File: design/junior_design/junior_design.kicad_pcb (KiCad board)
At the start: 2 copper layers, 28 parts, among them J1 MPLAB SNAP, J2 Screw_Terminal_01x04, J3 Conn_01x05, J4 Conn_01x03, J5 USB_C_Receptacle_USB2.0_16P, U2 INA128, U3 TLV76133DCY, U4 MCP6022

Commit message: Started PCB layout
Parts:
- added H1: MountingHole, MountingHole:MountingHole_2.7mm, F.Cu at (76.2, 76.2)
- added H2: MountingHole, MountingHole:MountingHole_2.7mm, F.Cu at (196.8, 76.2)
- added H3: MountingHole, MountingHole:MountingHole_2.7mm, F.Cu at (76.2, 158.8)
- added H4: MountingHole, MountingHole:MountingHole_2.7mm, F.Cu at (196.8, 158.8)
- added U100: PIC24FJ64GA002-I_SP, Package_DIP:DIP-28_W7.62mm, F.Cu at (131.4, 133.3)
- moved R190 78.9 mm to (75.7, 122.4)
- moved U190 75.2 mm to (88.9, 116.2)
- moved J100 74.1 mm to (197.6, 106.1)
- moved R191 73.1 mm to (79.4, 112.4), turned to 90 degrees
- moved U110 71.3 mm to (158.1, 144.8), turned to 180 degrees
- moved U130 68.3 mm to (131.4, 139.7)
- moved J111 64.8 mm to (168.3, 150.5), turned to 90 degrees
- moved RV131 63.8 mm to (127.0, 147.8), turned to -90 degrees
- moved C190 62.3 mm to (83.2, 116.2), turned to 90 degrees
- moved J121 56.9 mm to (169.5, 132.1), turned to 180 degrees
- moved J190 55.6 mm to (77.4, 113.1), turned to -90 degrees
- moved C191 55.5 mm to (90.8, 120.7), turned to 180 degrees
- moved C111 52.6 mm to (173.4, 148.6), turned to -90 degrees
- moved RV130 51.7 mm to (144.3, 150.4), turned to -90 degrees
- moved R133 51.2 mm to (127.5, 140.2)
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- renumbered C1 to C100, C2 to C101, C3 to C102, C7 to C110, C6 to C111, C9 to C121, C8 to C130, C4 to C190, C5 to C191, J1 to J100, J2 to J111, J3 to J120, J4 to J121, J5 to J190, R7 to R100, R6 to R101, R1 to R110, R2 to R130, R4 to R131, R3 to R132, R5 to R133, R8 to R190, R9 to R191, RV2 to RV130, RV1 to RV131, U2 to U110, U4 to U130, U3 to U190
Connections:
- J190 pad S1: unconnected-(J5-SHIELD-PadS1) -> GND
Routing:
- net GND: track 0.00 -> 22.1 mm, vias 0 -> 3
- net +5V: track 0.00 -> 14.9 mm
- net Net-(U100-AN1/VREF-/CN3/RA1): track 0.00 -> 12.5 mm
- net /LDCELL+: track 0.00 -> 10.4 mm
- net /LDCELL-: track 0.00 -> 10.4 mm
- net Net-(U100-AN0/VREF+/CN2/RA0): track 0.00 -> 9.94 mm
- net +3.3V: track 0.00 -> 8.37 mm
- net Net-(U100-AN5/C1IN+/RP3/SCL2/CN7/RB3): track 0.00 -> 7.93 mm
- net Net-(J190-CC2): track 0.00 -> 5.96 mm
- net Net-(J190-CC1): track 0.00 -> 4.09 mm, vias 0 -> 1
- net Net-(R110-Pad2): track 0.00 -> 3.96 mm
- net Net-(R110-Pad1): track 0.00 -> 3.94 mm
- added copper zone on F.Cu, net +3.3V
- added copper zone on F.Cu, net +5V
- added copper zone on B.Cu, net GND
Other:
- board outline added: 130.8 x 92.7 mm

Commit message: Finish routing PCB
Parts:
- added G***: LOGO, LOGO, F.Cu at (120.7, 88.3)
- added G***: LOGO, LOGO, B.Cu at (136.5, 116.8)
- J111: footprint Connector_Phoenix_MC:PhoenixContact_MCV_1,5_4-G-3.81_1x04_P3.81mm_Vertical -> Connector_Phoenix_MC:PhoenixContact_MC_1,5_4-G-3.81_1x04_P3.81mm_Horizontal
- moved C111 18.5 mm to (156.2, 155.6), turned to 180 degrees
- moved J111 16.3 mm to (154.4, 159.0), turned to 0 degrees
- moved J121 14.8 mm to (159.4, 121.3), turned to 90 degrees
- moved J120 14.0 mm to (134.6, 114.3)
- moved C121 10.8 mm to (160.7, 118.7), turned to 180 degrees
- moved C100 1.27 mm to (151.8, 122.6)
- moved C101 1.27 mm to (131.4, 122.6)
- moved R133 0.76 mm to (128.3, 140.2)
- moved C130 0.51 mm to (142.2, 139.7)
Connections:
- C121 pad 1: +3.3V -> +5V
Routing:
- net +5V: track 14.9 -> 103.9 mm, vias 0 -> 2
- net /~{RST}: track 0.00 -> 83.6 mm
- net /PGD: track 0.00 -> 66.6 mm
- net /PGC: track 0.00 -> 63.8 mm
- net +3.3V: track 8.37 -> 61.1 mm
- net /SCL0: track 0.00 -> 20.0 mm
- net /SDA0: track 0.00 -> 19.7 mm
- net GND: track 22.1 -> 35.2 mm, vias 3 -> 32
- net /LDCELL+: track 10.4 -> 22.5 mm
- net /LDCELL-: track 10.4 -> 18.4 mm
- net /ADC-: track 0.00 -> 5.49 mm
- net /ADC+: track 0.00 -> 4.66 mm
- net /PWM0: track 0.00 -> 4.45 mm
- net Net-(U100-~{MCLR}): track 0.00 -> 2.90 mm
- net Net-(R132-Pad1): track 0.00 -> 2.75 mm
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- added copper zone on F.Cu, net GND
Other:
- board text added: "HINKLE INC"

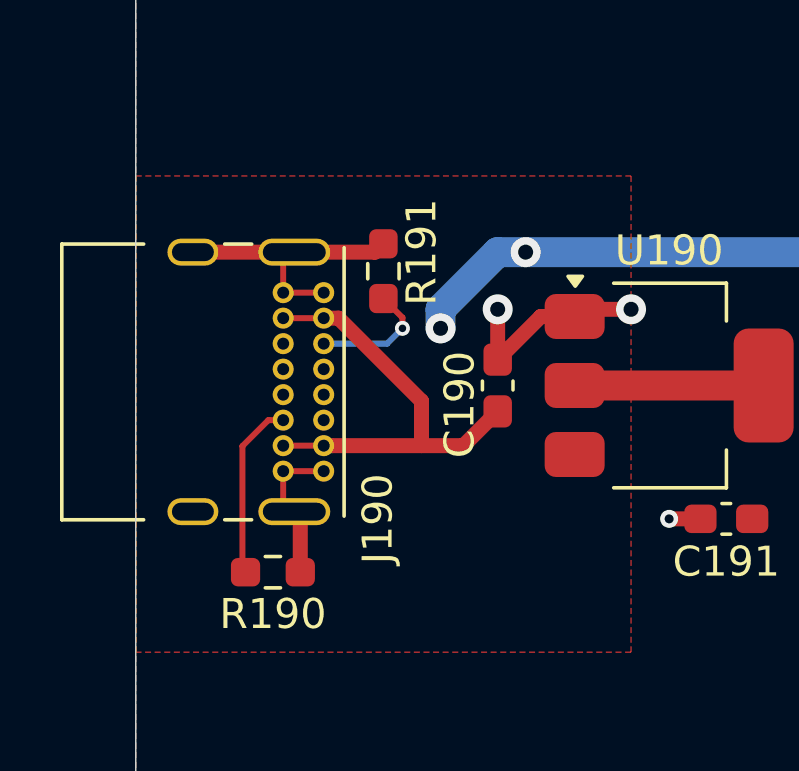
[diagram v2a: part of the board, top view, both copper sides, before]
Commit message: add ferrite beads to usb-c port
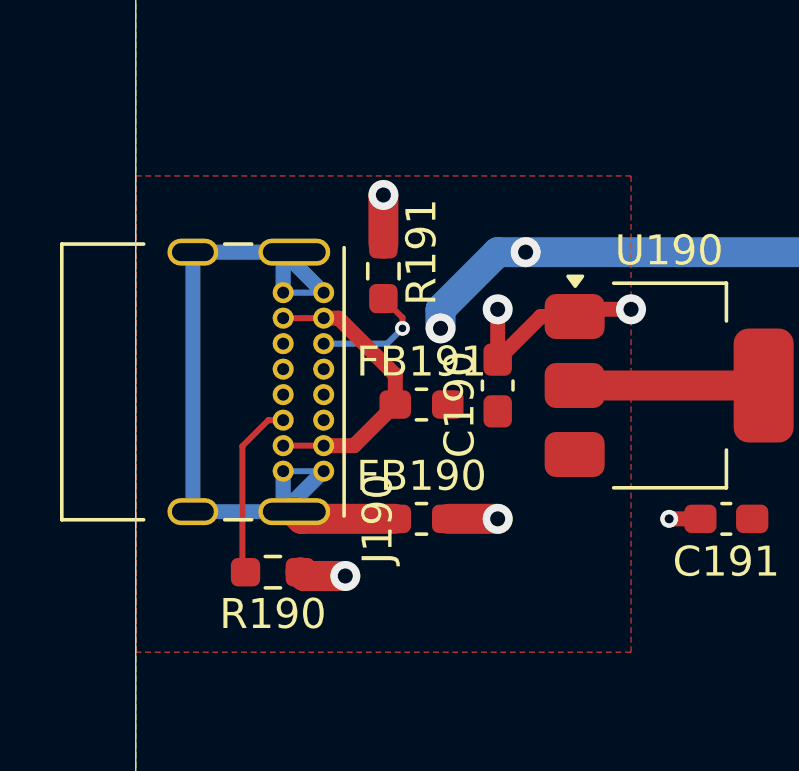
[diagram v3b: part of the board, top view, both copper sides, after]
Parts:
- added FB190: FerriteBead, Inductor_SMD:L_0603_1608Metric_Pad1.05x0.95mm_HandSolder, F.Cu at (80.6, 120.7)
- added FB191: FerriteBead, Inductor_SMD:L_0603_1608Metric_Pad1.05x0.95mm_HandSolder, F.Cu at (80.6, 116.8)
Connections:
- J190 pad A1: GND -> Net-(J190-SHIELD)
- J190 pad A12: GND -> Net-(J190-SHIELD)
- J190 pad A4: +5V -> Net-(FB191-Pad1)
- J190 pad A9: +5V -> Net-(FB191-Pad1)
- J190 pad B1: GND -> Net-(J190-SHIELD)
- J190 pad B12: GND -> Net-(J190-SHIELD)
- J190 pad B4: +5V -> Net-(FB191-Pad1)
- J190 pad B9: +5V -> Net-(FB191-Pad1)
- J190 pad S1: GND -> Net-(J190-SHIELD)
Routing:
- net Net-(J190-SHIELD): track 0.00 -> 28.1 mm
- net +5V: track 103.9 -> 88.7 mm
- net Net-(FB191-Pad1): track 0.00 -> 9.81 mm
- net GND: track 35.2 -> 25.8 mm, vias 32 -> 35
